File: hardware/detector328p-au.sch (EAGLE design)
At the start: 63 parts, among them J1 AVR_SPI_PRG_6NS, K1 SRD-05VDC-SL-C, Q1 BSS123, Q2 16MHz, T1 BC817-40SMD, T2 BC817, T3 BC817, U1 ATMEGA328P-AU

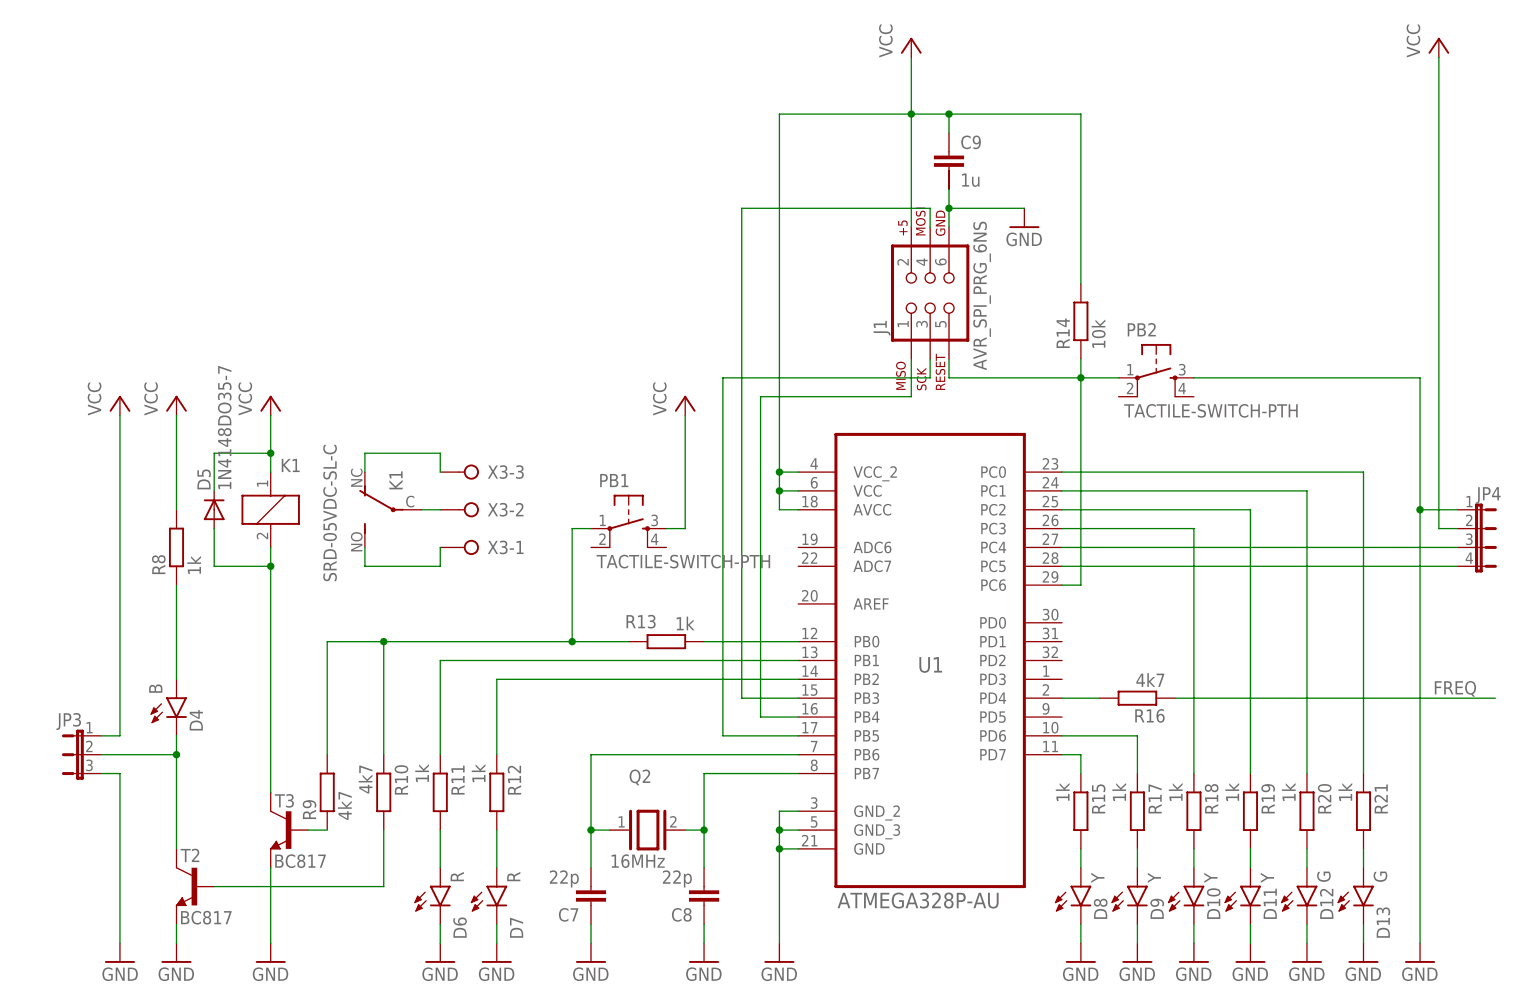
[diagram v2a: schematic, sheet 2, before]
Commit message: hardware-328p-au: more smt replacements
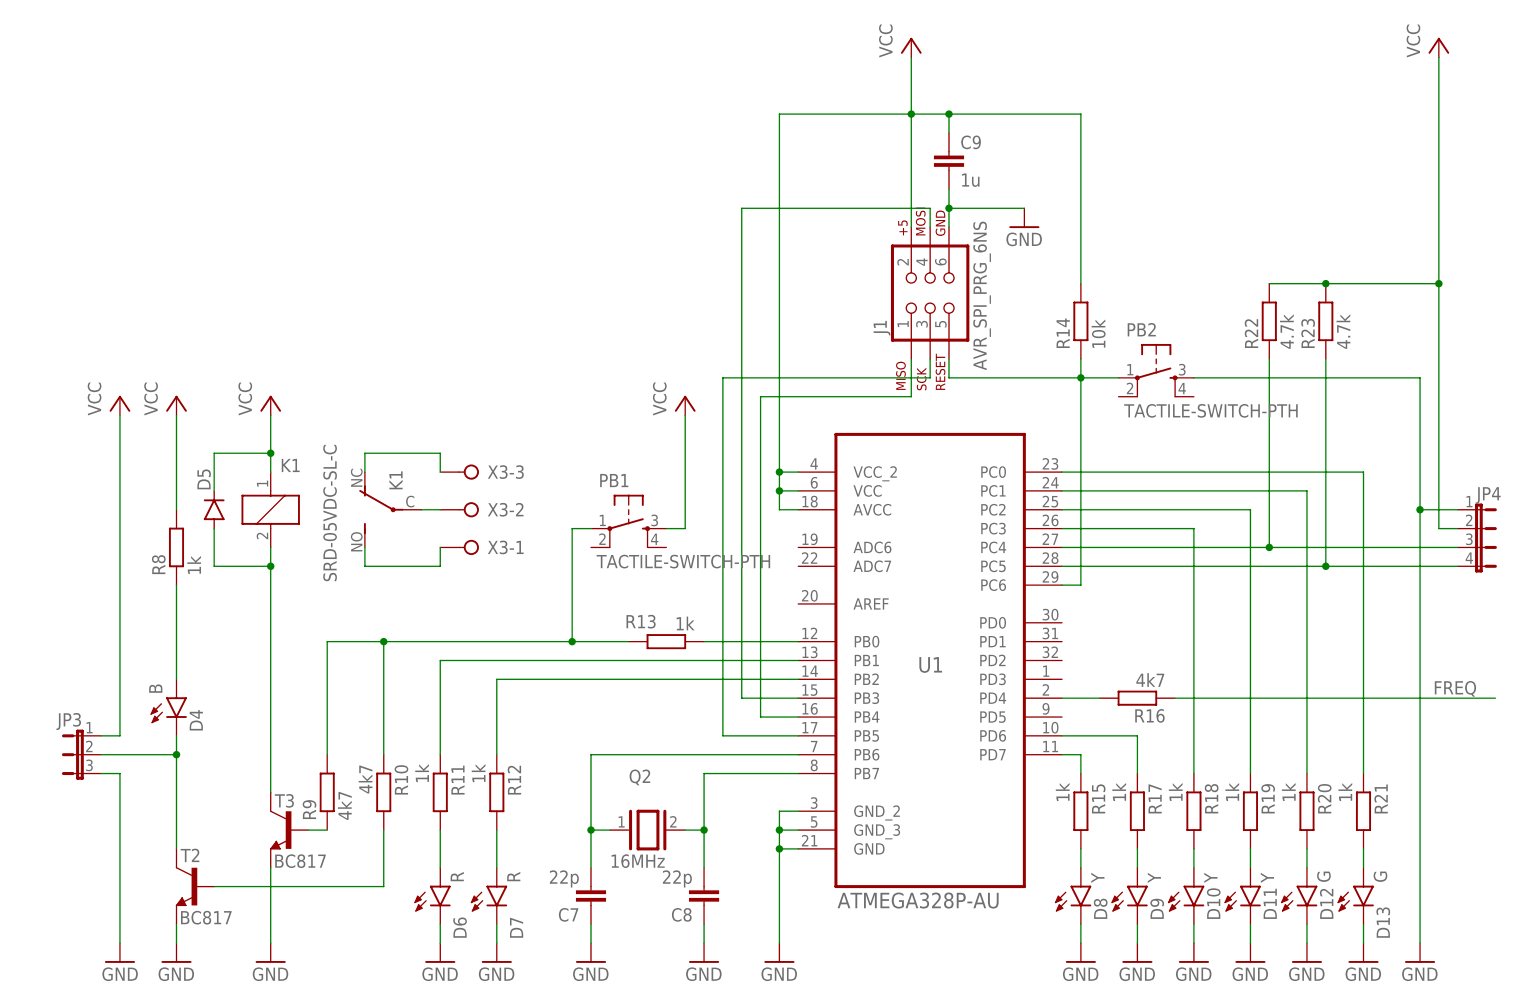
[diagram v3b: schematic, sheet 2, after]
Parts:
- added R22, R23: 4.7k, rcl:R-EU_R0603
- C1, C2, C3, C4: device resistor:C-EU050-024X044 -> resistor:C-EUC0603
- C5, C6, C9: device capacitor-wima:C-2.5-5/4 -> rcl:C-EUC0603
- D1, D2: value 24V -> 16V; device SparkFun-DiscreteSemi:DIODE-ZENER -> detector:DIODE-ZENER16V
- D5: value 1N4148DO35-7 -> (none); device diode:1N4148DO35-7 -> detector:DIODESOD123
- R5: device resistor:R-EU_0204/5 -> resistor:R-EU_R0603
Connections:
- net N$44: now also R23.1
- net N$45: now also R22.1
- net VCC: now also R22.2, R23.2
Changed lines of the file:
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@@
 <part name="R6" library="resistor" deviceset="R-EU_" device="R0603" value="1k"/>
 <part name="R2" library="resistor" deviceset="R-EU_" device="R0603" value="470"/>
-<part name="R5" library="resistor" deviceset="R-EU_" device="0204/5" value="4k7"/>
+<part name="R5" library="resistor" deviceset="R-EU_" device="R0603" value="4k7"/>
 <part name="Q1" library="transistor-small-signal" deviceset="BSS123" device=""/>
-<part name="C1" library="resistor" deviceset="C-EU" device="050-024X044" value="100n"/>
-<part name="C2" library="resistor" deviceset="C-EU" device="050-024X044" value="47n"/>
-<part name="C3" library="resistor" deviceset="C-EU" device="050-024X044" value="33n"/>
-<part name="C4" library="resistor" deviceset="C-EU" device="050-024X044" value="22n"/>
+<part name="C1" library="resistor" deviceset="C-EU" device="C0603" value="100n"/>
+<part name="C2" library="resistor" deviceset="C-EU" device="C0603" value="47n"/>
+<part name="C3" library="resistor" deviceset="C-EU" device="C0603" value="33n"/>
+<part name="C4" library="resistor" deviceset="C-EU" device="C0603" value="22n"/>
 <part name="GND5" library="supply1" deviceset="GND" device=""/>
 <part name="P+1" library="supply1" deviceset="VCC" device=""/>
@@
 <part name="R4" library="resistor" deviceset="R-EU_" device="R0603" value="150"/>
 <part name="GND6" library="supply1" deviceset="GND" device=""/>
-<part name="D1" library="SparkFun-DiscreteSemi" deviceset="DIODE-ZENER" device="" value="24V"/>
-<part name="D2" library="SparkFun-DiscreteSemi" deviceset="DIODE-ZENER" device="" value="24V"/>
+<part name="D1" library="detector" deviceset="DIODE-ZENER" device="16V" value="16V"/>
+<part name="D2" library="detector" deviceset="DIODE-ZENER" device="16V" value="16V"/>
 <part name="GND-ISO1" library="SparkFun-Aesthetics" deviceset="GND-ISO" device=""/>
 <part name="R1" library="resistor" deviceset="R-EU_" device="R0603" value="1M8"/>
@@
 <part name="X2" library="con-wago-500" deviceset="W237-102" device=""/>
 <part name="L1" library="detector" deviceset="78601/9C" device=""/>
-<part name="C5" library="capacitor-wima" deviceset="C-" device="2.5-5/4" value="1u"/>
+<part name="C5" library="rcl" deviceset="C-EU" device="C0603" value="1u"/>
 <part name="GND7" library="supply1" deviceset="GND" device=""/>
-<part name="C6" library="capacitor-wima" deviceset="C-" device="2.5-5/4" value="1u"/>
+<part name="C6" library="rcl" deviceset="C-EU" device="C0603" value="1u"/>
 <part name="R10" library="resistor" deviceset="R-EU_" device="R0603" value="4k7"/>
 <part name="R15" library="resistor" deviceset="R-EU_" device="R0603" value="1k"/>
@@
 <part name="GND16" library="supply1" deviceset="GND" device=""/>
 <part name="GND17" library="supply1" deviceset="GND" device=""/>
-<part name="C9" library="capacitor-wima" deviceset="C-" device="2.5-5/4" value="1u"/>
+<part name="C9" library="rcl" deviceset="C-EU" device="C0603" value="1u"/>
 <part name="R17" library="resistor" deviceset="R-EU_" device="R0603" value="1k"/>
 <part name="D9" library="SparkFun-LED" deviceset="LED" device="0603" value="Y"/>
@@
 <part name="P+6" library="supply1" deviceset="VCC" device=""/>
 <part name="R9" library="resistor" deviceset="R-EU_" device="R0603" value="4k7"/>
-<part name="D5" library="diode" deviceset="1N4148" device="DO35-7"/>
+<part name="D5" library="detector" deviceset="DIODE" device="SOD123"/>
 <part name="X3" library="con-wago-508" deviceset="W237-03P" device=""/>
 <part name="JP4" library="jumper" deviceset="JP4E" device=""/>
@@
 <part name="R3" library="resistor" deviceset="R-EU_" device="R0603" value="150"/>
 <part name="T2" library="transistor-npn" deviceset="BC817*" device="SMD" technology="-40" value="BC817"/>
+<part name="R22" library="rcl" deviceset="R-EU_" device="R0603" value="4.7k"/>
+<part name="R23" library="rcl" deviceset="R-EU_" device="R0603" value="4.7k"/>
 </parts>
 <sheets>
@@
 <instance part="D1" gate="G$1" x="73.66" y="50.8" smashed="yes" rot="R270">
 <attribute name="NAME" x="69.0626" y="53.34" size="1.778" layer="95" rot="R270"/>
-<attribute name="VALUE" x="76.4286" y="53.34" size="1.778" layer="96" rot="R270"/>
 </instance>
 <instance part="D2" gate="G$1" x="73.66" y="40.64" smashed="yes" rot="R90">
 <attribute name="NAME" x="70.6374" y="38.1" size="1.778" layer="95" rot="R90"/>
-<attribute name="VALUE" x="78.5114" y="38.1" size="1.778" layer="96" rot="R90"/>
 </instance>
 <instance part="GND-ISO1" gate="G$1" x="33.02" y="10.16"/>
@@
 <attribute name="VALUE" x="25.4" y="15.24" size="1.778" layer="96" rot="MR0"/>
 </instance>
+<instance part="R22" gate="G$1" x="165.1" y="96.52" rot="R90"/>
+<instance part="R23" gate="G$1" x="172.72" y="96.52" rot="R90"/>
 </instances>
 <busses>
@@
 <pinref part="P+9" gate="VCC" pin="VCC"/>
 <wire x1="190.5" y1="68.58" x2="187.96" y2="68.58" width="0.1524" layer="91"/>
-<wire x1="187.96" y1="68.58" x2="187.96" y2="132.08" width="0.1524" layer="91"/>
+<wire x1="187.96" y1="68.58" x2="187.96" y2="101.6" width="0.1524" layer="91"/>
+<pinref part="R22" gate="G$1" pin="2"/>
+<pinref part="R23" gate="G$1" pin="2"/>
+<wire x1="187.96" y1="101.6" x2="187.96" y2="132.08" width="0.1524" layer="91"/>
+<wire x1="165.1" y1="101.6" x2="172.72" y2="101.6" width="0.1524" layer="91"/>
+<wire x1="172.72" y1="101.6" x2="187.96" y2="101.6" width="0.1524" layer="91"/>
+<junction x="172.72" y="101.6"/>
+<junction x="187.96" y="101.6"/>
 </segment>
 <segment>
@@
 <pinref part="JP4" gate="G$1" pin="4"/>
 <pinref part="U1" gate="A" pin="PC5"/>
-<wire x1="190.5" y1="63.5" x2="137.16" y2="63.5" width="0.1524" layer="91"/>
+<wire x1="190.5" y1="63.5" x2="172.72" y2="63.5" width="0.1524" layer="91"/>
+<pinref part="R23" gate="G$1" pin="1"/>
+<wire x1="172.72" y1="63.5" x2="137.16" y2="63.5" width="0.1524" layer="91"/>
+<wire x1="172.72" y1="91.44" x2="172.72" y2="63.5" width="0.1524" layer="91"/>
+<junction x="172.72" y="63.5"/>
 </segment>
 </net>
@@
 <pinref part="U1" gate="A" pin="PC4"/>
 <pinref part="JP4" gate="G$1" pin="3"/>
-<wire x1="137.16" y1="66.04" x2="190.5" y2="66.04" width="0.1524" layer="91"/>
-</segment>
-</net>
+<wire x1="137.16" y1="66.04" x2="165.1" y2="66.04" width="0.1524" layer="91"/>
+<pinref part="R22" gate="G$1" pin="1"/>
+<wire x1="165.1" y1="66.04" x2="190.5" y2="66.04" width="0.1524" layer="91"/>
+<wire x1="165.1" y1="66.04" x2="165.1" y2="91.44" width="0.1524" layer="91"/>
+<junction x="165.1" y="66.04"/>
+</segment>
+</net>

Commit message: Board level 0
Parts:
- D1, D2: value 16V -> 5.1V 0.5W; device detector:DIODE-ZENER16V -> diode:ZENER-DIODESOD80C
- D5: device detector:DIODESOD123 -> diode:DIODE-SOD80C
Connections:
- net N$21: now also X1-1.KL; no longer X1-3.KL
- net N$7: now also X1-3.KL; no longer X1-1.KL
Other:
- moved on the sheet: X1-1, X1-2, X1-3

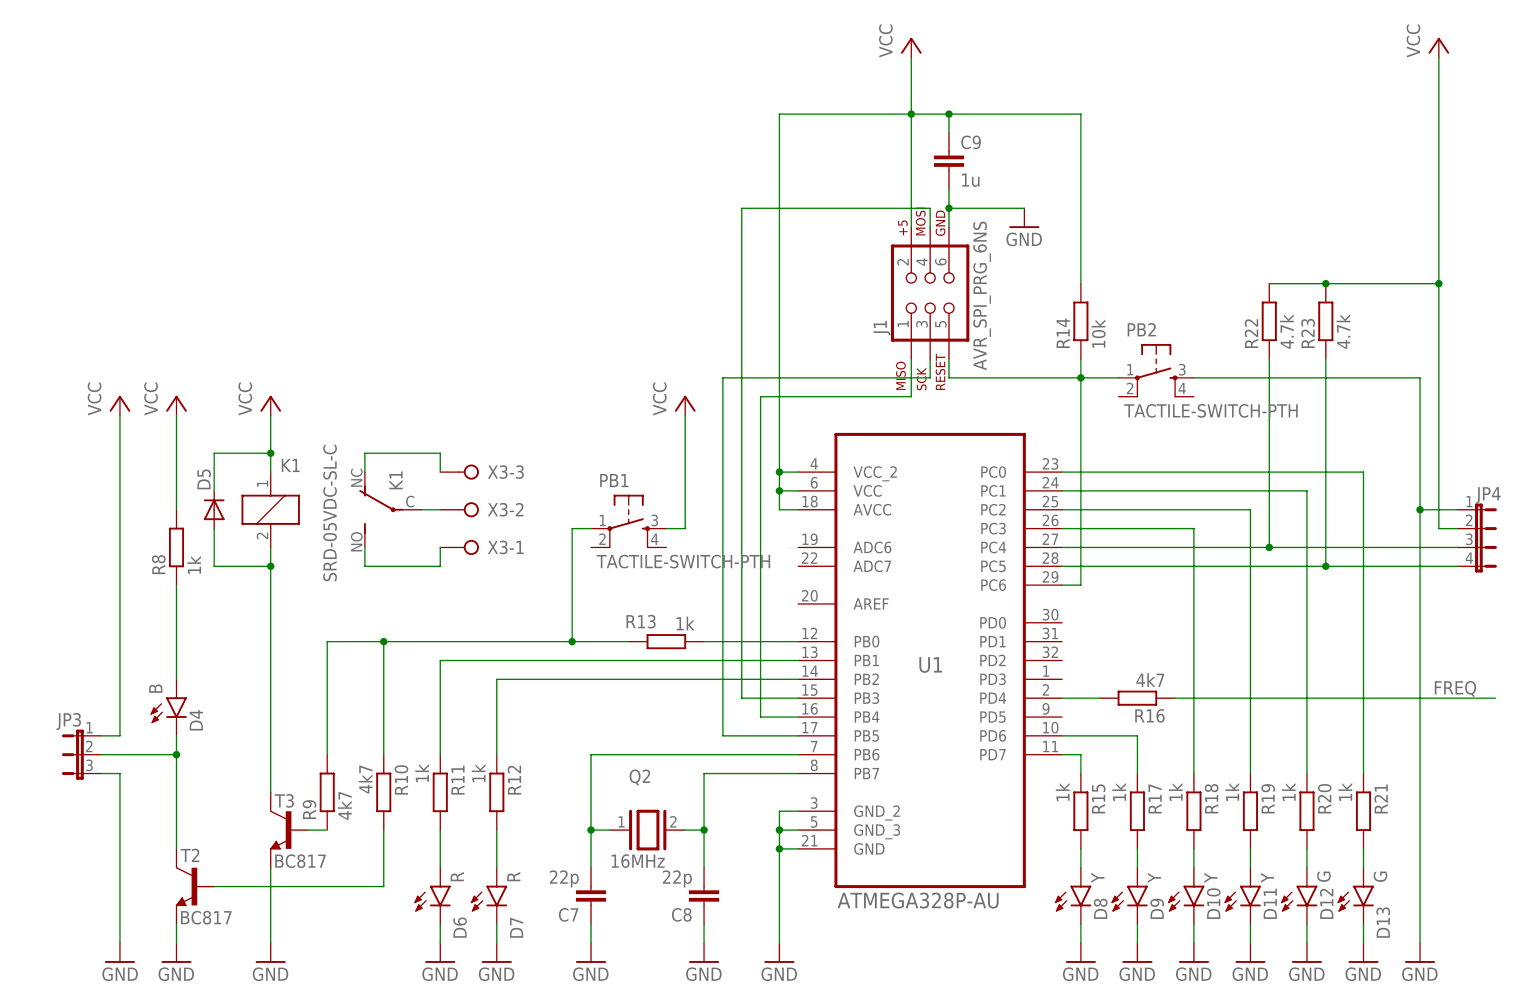
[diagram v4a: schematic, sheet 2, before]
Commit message: detector328p-au level 1: devices at place
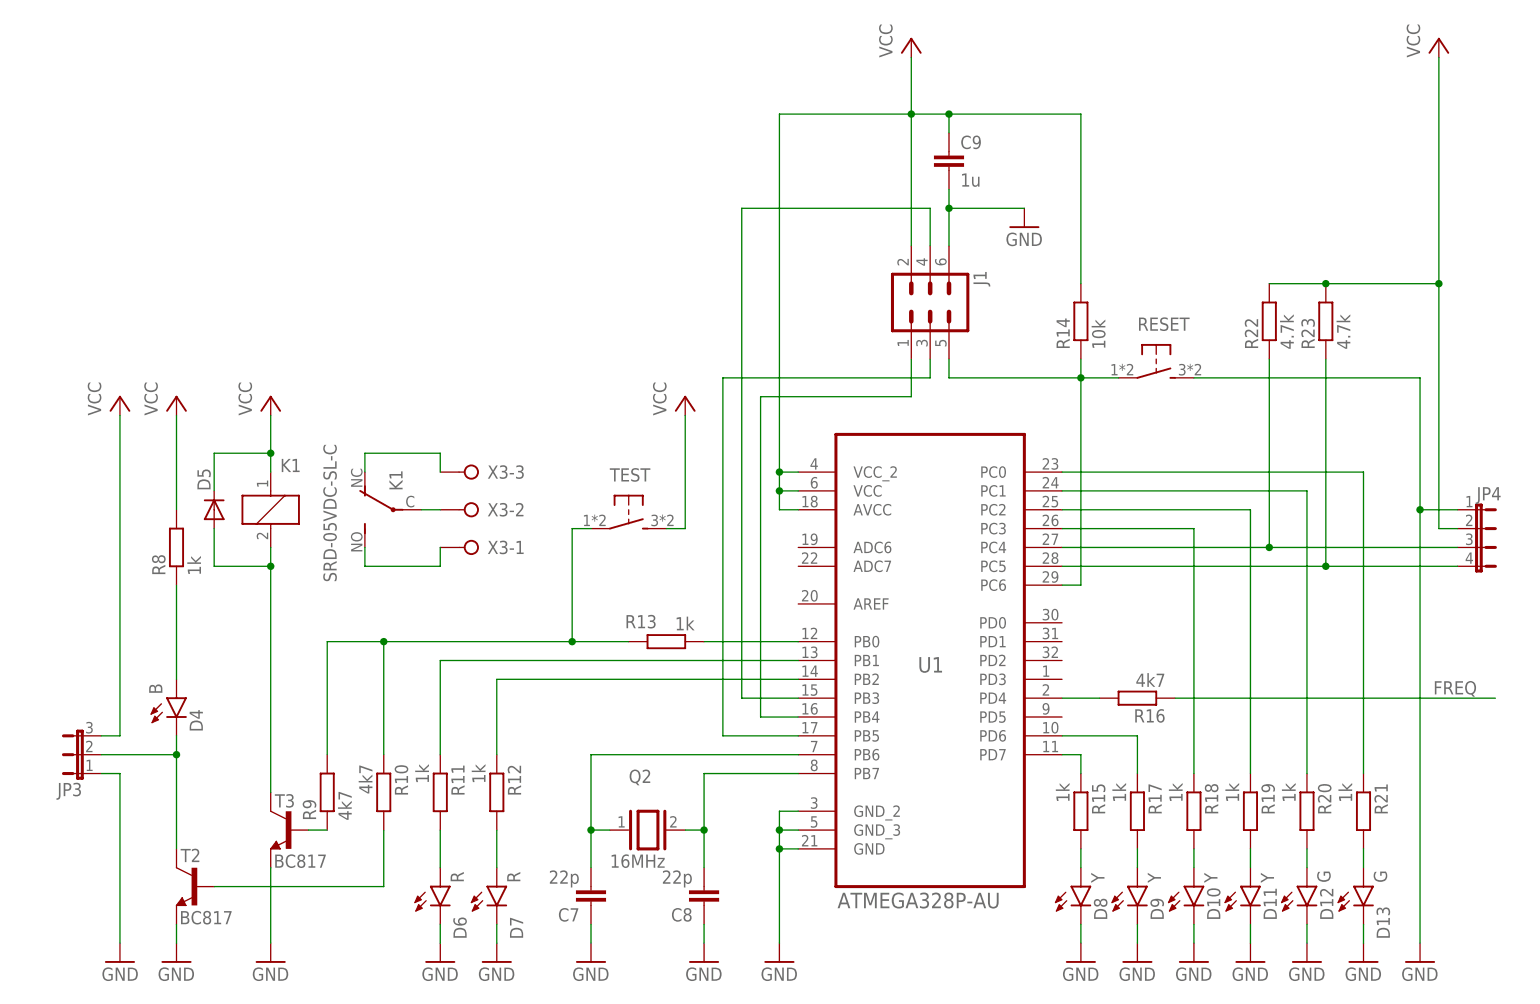
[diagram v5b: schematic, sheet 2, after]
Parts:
- removed PB1, PB2: TACTILE-SWITCH-PTH, GeekAmmo:TACTILE-SWITCH-PTH
- added RESET, TEST: (no value), detector:10-XX
- J1: value AVR_SPI_PRG_6NS -> (none); device SparkFun-Connectors:AVR_SPI_PRG_6NS -> con-lstb:MA03-2
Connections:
- net GND: now also JP3.1, RESET.S; no longer JP3.3, PB2.3
- net N$30: now also RESET.P; no longer PB2.1
- net N$47: now also TEST.P; no longer PB1.1
- net VCC: now also JP3.3, TEST.S; no longer JP3.1, PB1.3
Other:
- moved on the sheet: JP3
